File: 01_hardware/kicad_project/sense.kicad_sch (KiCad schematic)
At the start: 22 parts, among them U7 INA181A1IDBVR, U8 INA181A2IDBVR

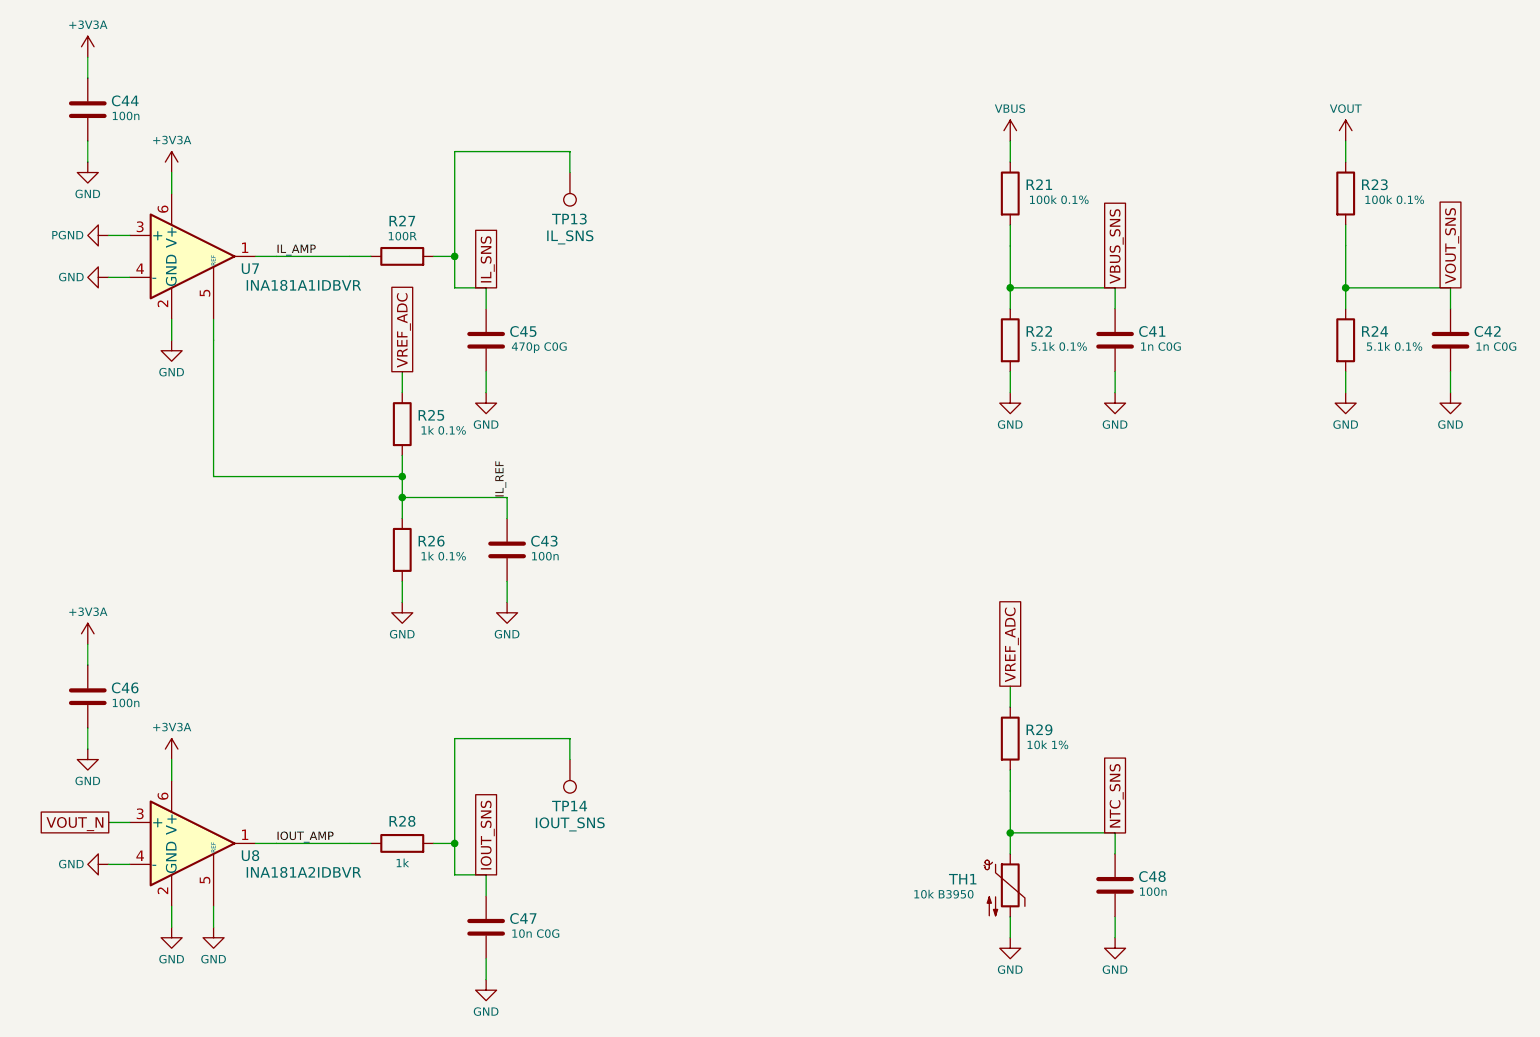
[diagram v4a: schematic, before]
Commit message: Rev E: isolated flyback aux supply, VREF+ back to 3.3 V, 1 oz re-layout
- New isolated aux flyback (sheet iso_pwr): UC3843B U20 from +10V_P, FDN86246 Q11,
  PA3855.006NLT EP13 T2, SS110 D9 -> isolated +10 V; secondary regulation TL431 U22 +
  EL357N opto U21 into COMP; RCD clamp D8/R116/C94; 2 A primary limit (R114)
- Secondary rails from the flyback, not VBUS: +10 V -> U4 10->5 V -> U5 TLV75533 3.3 V;
  MCU, CAN and drivers up before the LLC starts
- U12 -> CA-IS3742LW (data only); REF3030 U19 removed, VREF+ = +3V3A (3.3 V full scale)
- PCB re-placed / re-routed for 1 oz outer / 0.5 oz inner: power pours on F.Cu, In1 solid
  ground planes, gate loops as tight HO/HS pairs, 1.7 mm power-via pitch, per-pad GND vias
  in the MCU area; copper loss ~0.5 W at 50 W (03_calculations/copper_check.txt)
- DRC (JLC rules) 0 errors / 0 unconnected; netlist 148 nets / 284 parts 0 errors;
  isolation bands clear; BOM / JLC BOM+CPL / Gerbers / PDFs / design notes / READMEs updated
- Scripts: 04_scripts/pcb5 (placement, pours, routing, floods, island vias, silk),
  03_calculations/flyback_aux.py, copper_check.py

Co-Authored-By: Claude Opus 5.5 <noreply@anthropic.com>
Claude-Session: https://claude.ai/code/session_01A35wrnwFKLPSaRSxxHs471
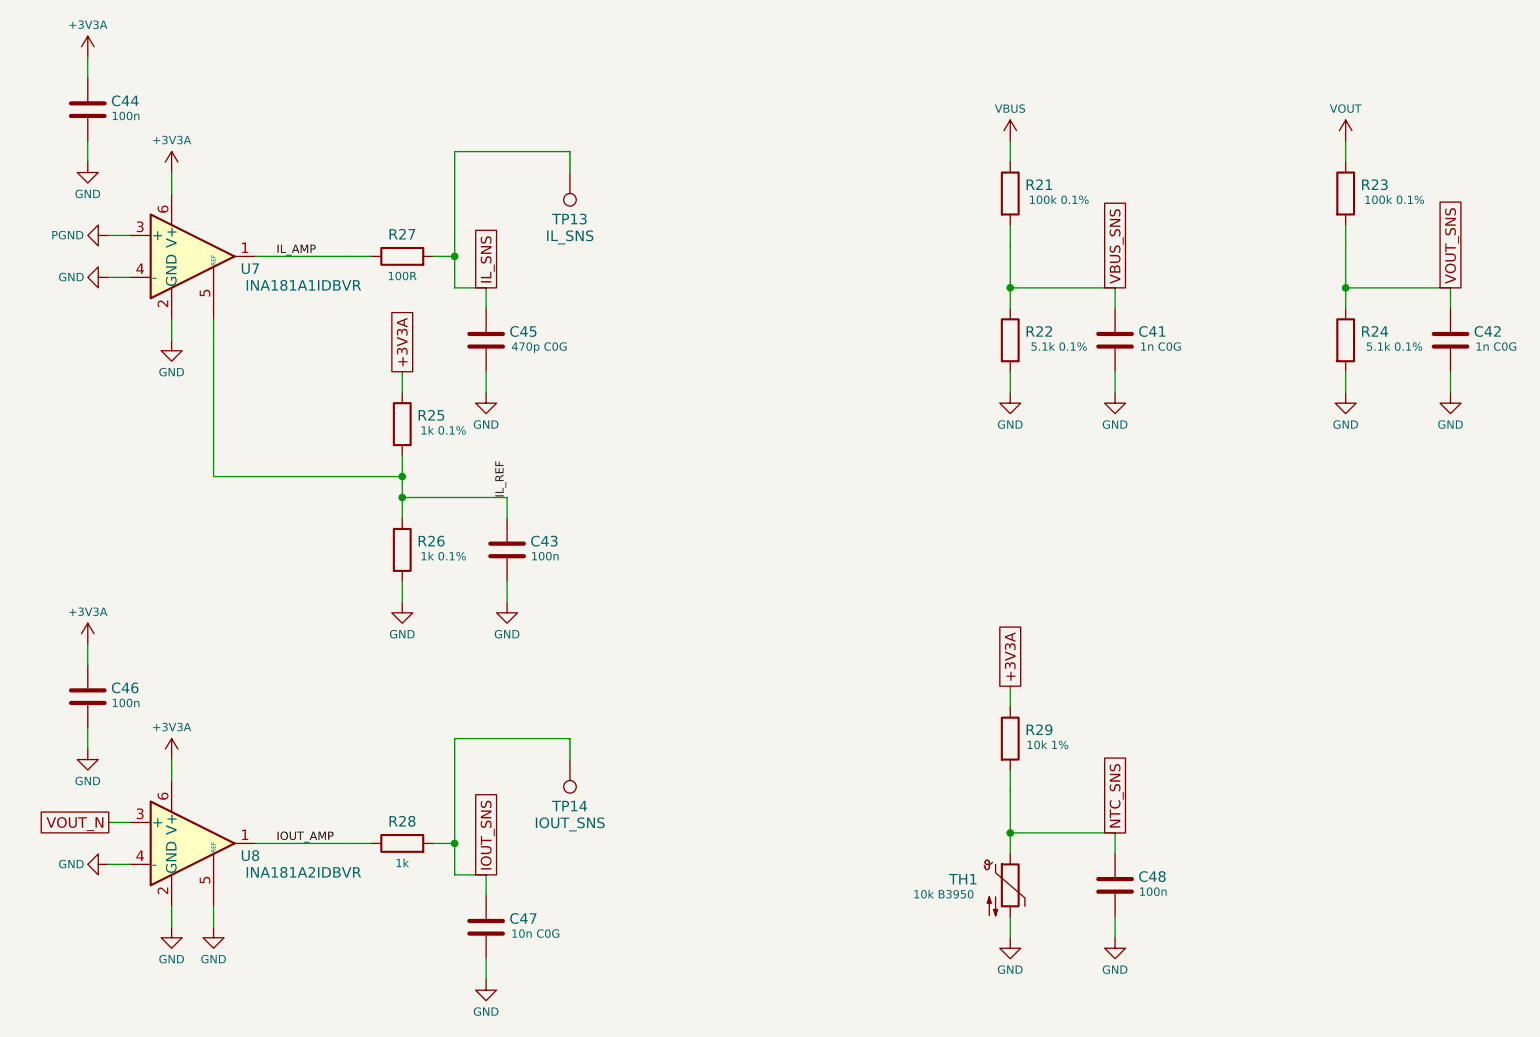
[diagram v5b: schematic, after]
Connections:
- net VREF_ADC is gone; now on net +3V3A: R25.1, R29.1
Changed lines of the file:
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@@
   (title_block
     (title "Sensing - VBUS, VOUT, inductor and output current, NTC")
-    (date "2026-10-18")
-    (rev "D")
+    (date "2026-10-19")
+    (rev "E")
     (comment 1 "DCDC LLC + 4SBB, 12-48 V in, 1.5-48 V / 5 A out, STM32G474")
-    (comment 2 "Sheet 7: Sensing - VBUS, VOUT, inductor and output current, NTC")
+    (comment 2 "Sheet 8: Sensing - VBUS, VOUT, inductor and output current, NTC")
   )
   (junction (at 132.08 107.95) (diameter 0) (color 0 0 0 0)
@@
     )
   )
-  (global_label "VREF_ADC" (shape passive) (at 132.08 95.25 90)
+  (global_label "+3V3A" (shape passive) (at 132.08 95.25 90)
     (effects (font (size 1.27 1.27)) (justify left))
     (property "Intersheet References" "${INTERSHEET_REFS}" (id 0) (at 132.08 95.25 0)
@@
     )
   )
-  (global_label "VREF_ADC" (shape passive) (at 205.74 133.35 90)
+  (global_label "+3V3A" (shape passive) (at 205.74 133.35 90)
     (effects (font (size 1.27 1.27)) (justify left))
     (property "Intersheet References" "${INTERSHEET_REFS}" (id 0) (at 205.74 133.35 0)
@@
   (symbol (lib_id "Device:R") (at 132.08 81.28 90) (unit 1)
     (in_bom yes) (on_board yes)
-    (property "Reference" "R27" (id 0) (at 132.08 77.048 90)
-      (effects (font (size 1.27 1.27)))
-    )
-    (property "Value" "100R" (id 1) (at 132.08 78.864 90)
-      (effects (font (size 1.0 1.0)))
-    )
+    (property "Reference" "R27" (id 0) (at 132.08 78.648 90)
+      (effects (font (size 1.27 1.27)))
+    )
+    (property "Value" "100R" (id 1) (at 132.08 83.696 90)
+      (effects (font (size 1.0 1.0)))
+    )

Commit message: Rev E BOM: in-stock LCSC first source for every part; 2nd/3rd sources checked
- First sources swapped (same footprints, layout unchanged): U1 STM32G474RBT3,
  Q2/Q3/Q5/Q6 NCEP068N10G, 10k 0402 FOJAN, 100n 0402 merged onto C307331,
  1u 0402 CCTC, R62/R63/R89/R82, FB1 Murata BLM18KG601SN1D, L2/L3 cjiang
  FNR5040S470MT, C82 KEMET C0G (was X7R), RS1 Milliohm HoJLR2512, SS110 MDD
- LCSC part numbers for the hand-soldered headers (J1-J5, J7, JP1)
- Schematic and PCB fields, BOM, JLC BOM/CPL, PDFs and design notes regenerated;
  netlist check 0 errors, DRC unchanged
- BOM_sourcing_revE.xlsx: live LCSC stock 2026-10-20, 2nd/3rd sources checked
  for pinout / land pattern / ratings, PCB reserve options for T2 and U9

Co-Authored-By: Claude Opus 5.5 <noreply@anthropic.com>
Claude-Session: https://claude.ai/code/session_01A35wrnwFKLPSaRSxxHs471
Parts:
- C43, C44, C46, C48: LCSC C1525 -> C307331
- R29: LCSC C25744 -> C2906861
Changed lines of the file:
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@@
       (effects (font (size 1.27 1.27)) hide)
     )
-    (property "LCSC" "C1525" (id 4) (at 144.78 116.84 0)
+    (property "LCSC" "C307331" (id 4) (at 144.78 116.84 0)
       (effects (font (size 1.27 1.27)) hide)
     )
@@
       (effects (font (size 1.27 1.27)) hide)
     )
-    (property "LCSC" "C1525" (id 4) (at 93.98 63.5 0)
+    (property "LCSC" "C307331" (id 4) (at 93.98 63.5 0)
       (effects (font (size 1.27 1.27)) hide)
     )
@@
       (effects (font (size 1.27 1.27)) hide)
     )
-    (property "LCSC" "C1525" (id 4) (at 93.98 134.62 0)
+    (property "LCSC" "C307331" (id 4) (at 93.98 134.62 0)
       (effects (font (size 1.27 1.27)) hide)
     )
@@
       (effects (font (size 1.27 1.27)) hide)
     )
-    (property "LCSC" "C25744" (id 4) (at 205.74 139.7 0)
+    (property "LCSC" "C2906861" (id 4) (at 205.74 139.7 0)
       (effects (font (size 1.27 1.27)) hide)
     )
@@
       (effects (font (size 1.27 1.27)) hide)
     )
-    (property "LCSC" "C1525" (id 4) (at 218.44 157.48 0)
-      (effects (font (size 1.27 1.27)) hide)
-    )
+    (property "LCSC" "C307331" (id 4) (at 218.44 157.48 0)
+      (effects (font (size 1.27 1.27)) hide)
+    )
